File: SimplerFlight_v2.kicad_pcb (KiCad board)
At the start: 4 copper layers, 96 x 73.5 mm, 121 parts, among them J1 Battery 1, J10 Cam 1, J11 Servo, J12 Cam 1, J13 SWD Header, J14 DM3CS-SF, J2 Encoder, J7 Battery 2, J8 USB, J9 Cam 1, Q2 NPN, Q5 BSS816NWH6327XTSA1, Q6 BSS816NWH6327XTSA1, Q7 BSS816NWH6327XTSA1, SW1 Boot Switch, SW2 System Reset, U1 AMS1117-3.3, U2 STM32F401RETx, U3 BMP581, U4 BNO085, U5 TPS56A37RPAR, U6 TPS56A37RPAR, U7 MX25V4006EM1I-13G, Y2 Crystal

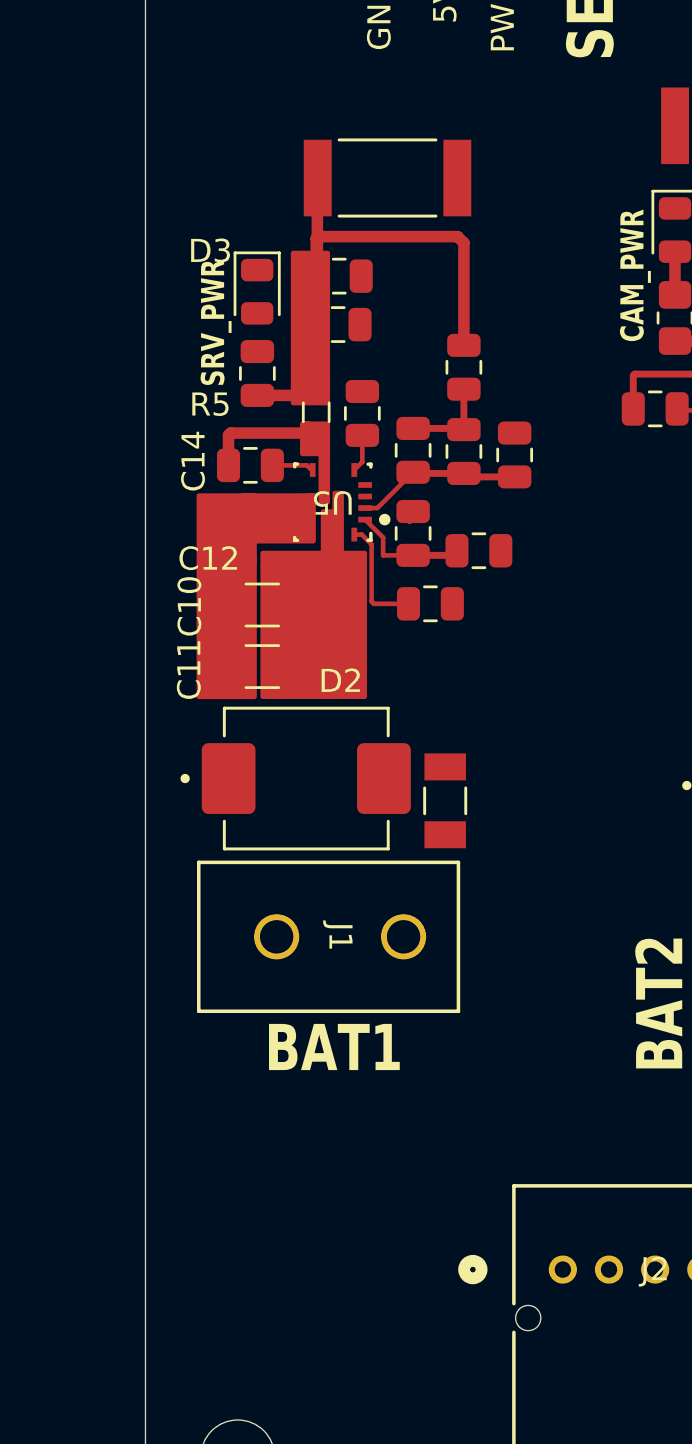
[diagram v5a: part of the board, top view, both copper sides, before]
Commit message: Update Cinx for servo motor power supply
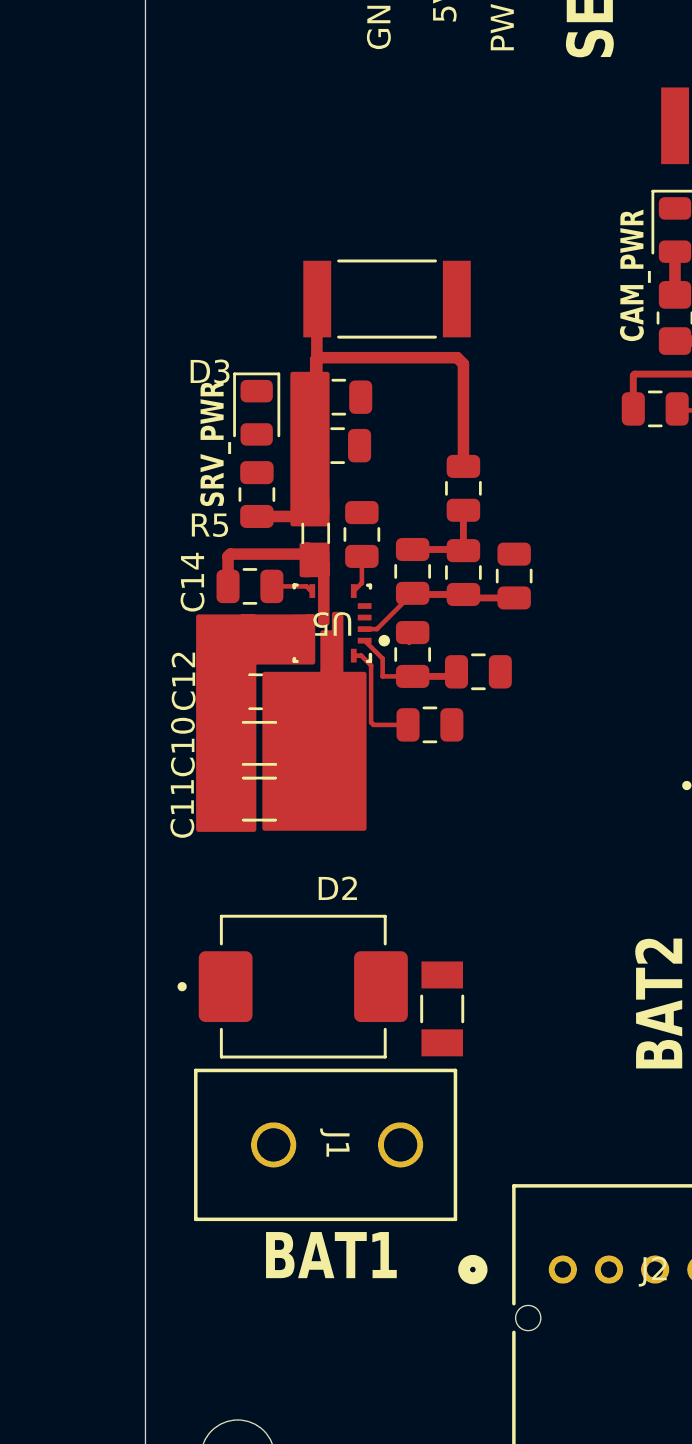
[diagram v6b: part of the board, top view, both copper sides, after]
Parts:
- C12: footprint Capacitor_SMD:C_0201_0603Metric -> Capacitor_SMD:C_0805_2012Metric
- moved F1 9.02 mm to (157.9, 124.6)
- moved J1 9.02 mm to (156.1, 130.5)
- moved D2 9.02 mm to (151.8, 123.6)
- moved C10 6.00 mm to (149.9, 113.1)
- moved C11 5.74 mm to (149.9, 115.5)
- moved C12 5.70 mm to (149.8, 110.8)
- moved C13 5.25 mm to (154.4, 104.0)
- moved C15 5.25 mm to (153.3, 100.2)
- moved C16 5.25 mm to (153.4, 98.1)
- moved D3 5.25 mm to (149.8, 98.8)
- moved L1 5.25 mm to (152.4, 104.0)
- moved R10 5.25 mm to (156.6, 105.6)
- moved R11 5.25 mm to (161.0, 105.8)
- moved R28 5.25 mm to (155.5, 93.8)
- moved R5 5.25 mm to (149.8, 102.3)
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
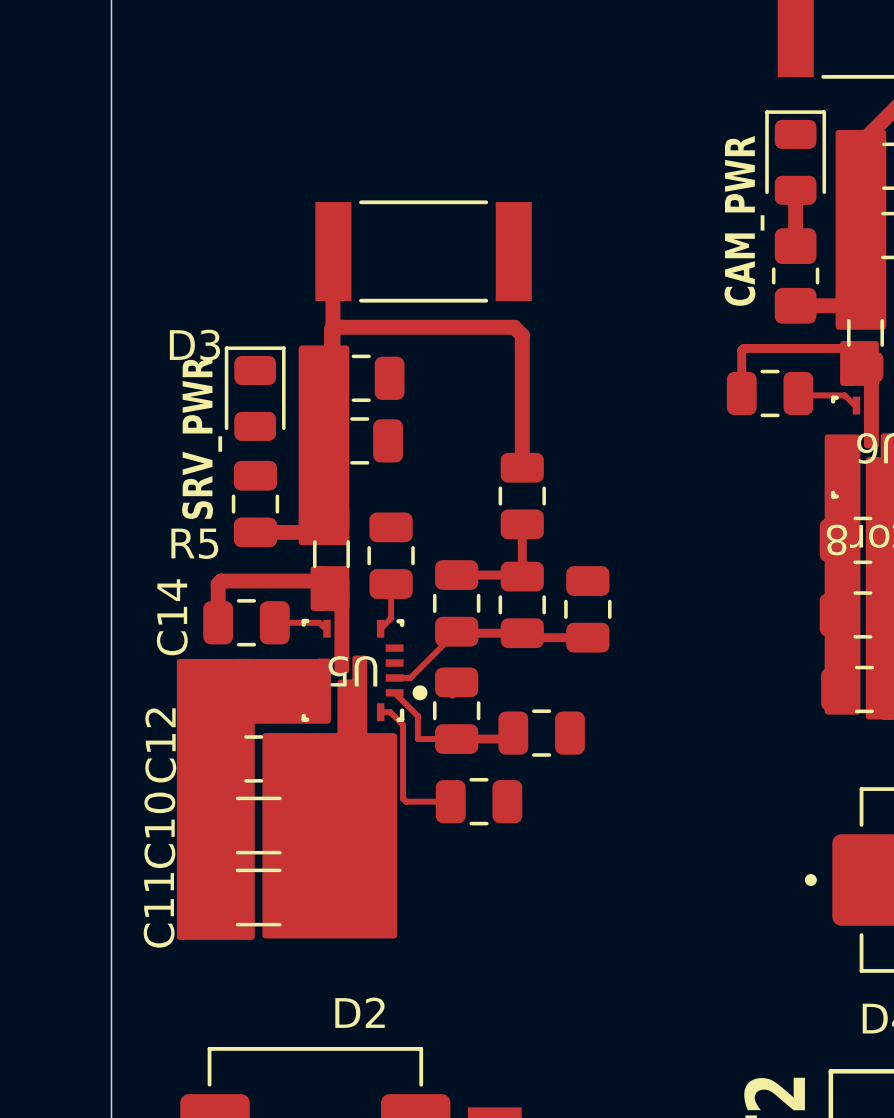
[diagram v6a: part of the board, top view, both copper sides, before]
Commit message: Update Cout models for servo motor power and extended pground
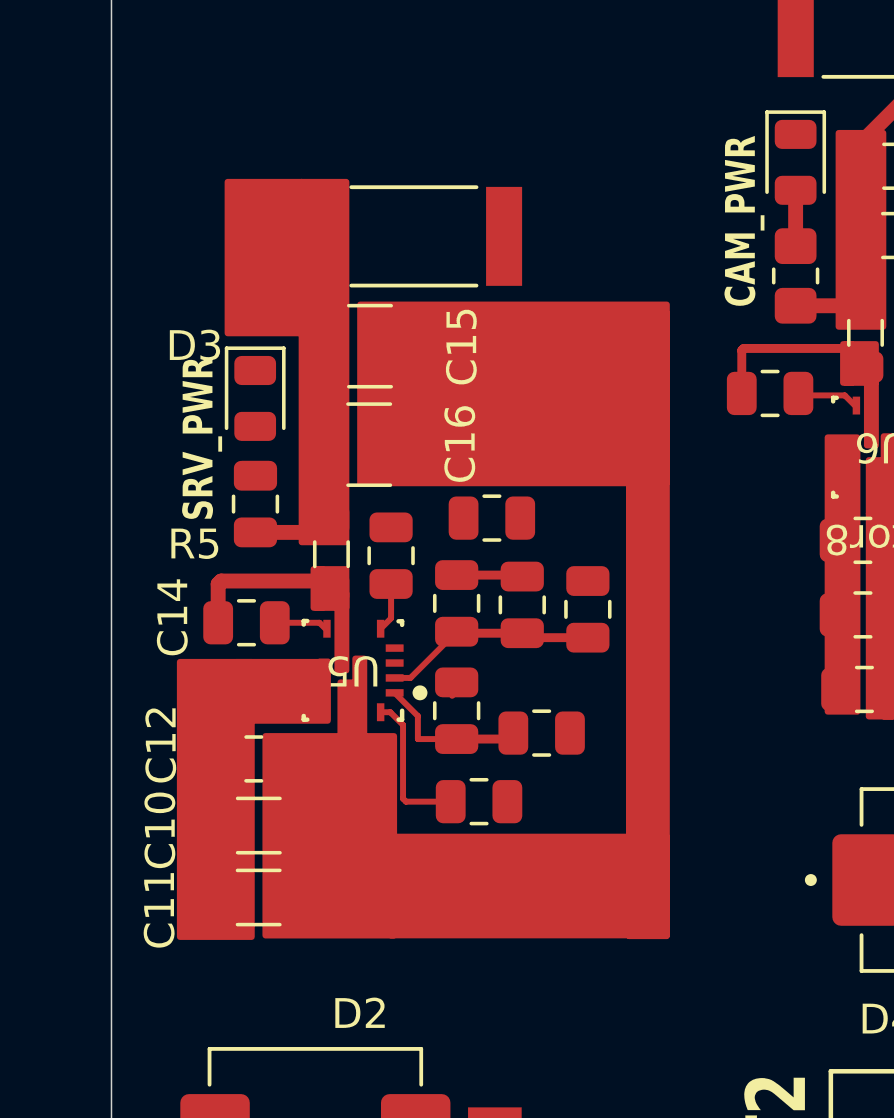
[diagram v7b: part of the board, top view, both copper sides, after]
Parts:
- C15, C16: footprint Capacitor_SMD:C_0805_2012Metric -> Capacitor_SMD:C_1210_3225Metric
- moved C15 3.20 mm to (153.7, 97.0)
- moved C16 2.24 mm to (153.6, 100.3)
- moved R9 1.26 mm to (157.8, 102.8), turned to 0 degrees
- moved R28 0.60 mm to (155.1, 93.3)
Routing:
- net /Power/5V_SERVO: track 21.7 -> 2.72 mm
- net Net-(C17-Pad1): track 3.97 -> 2.22 mm

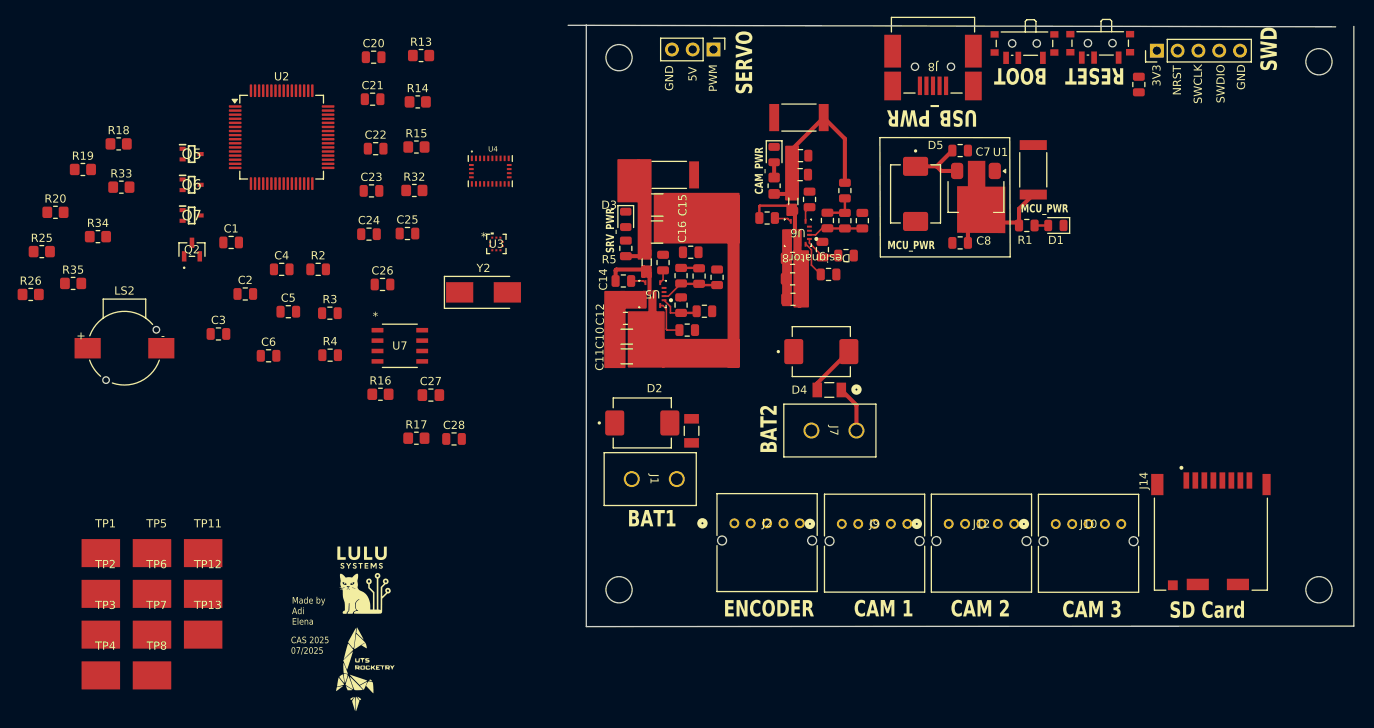
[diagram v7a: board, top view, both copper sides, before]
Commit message: update inductor
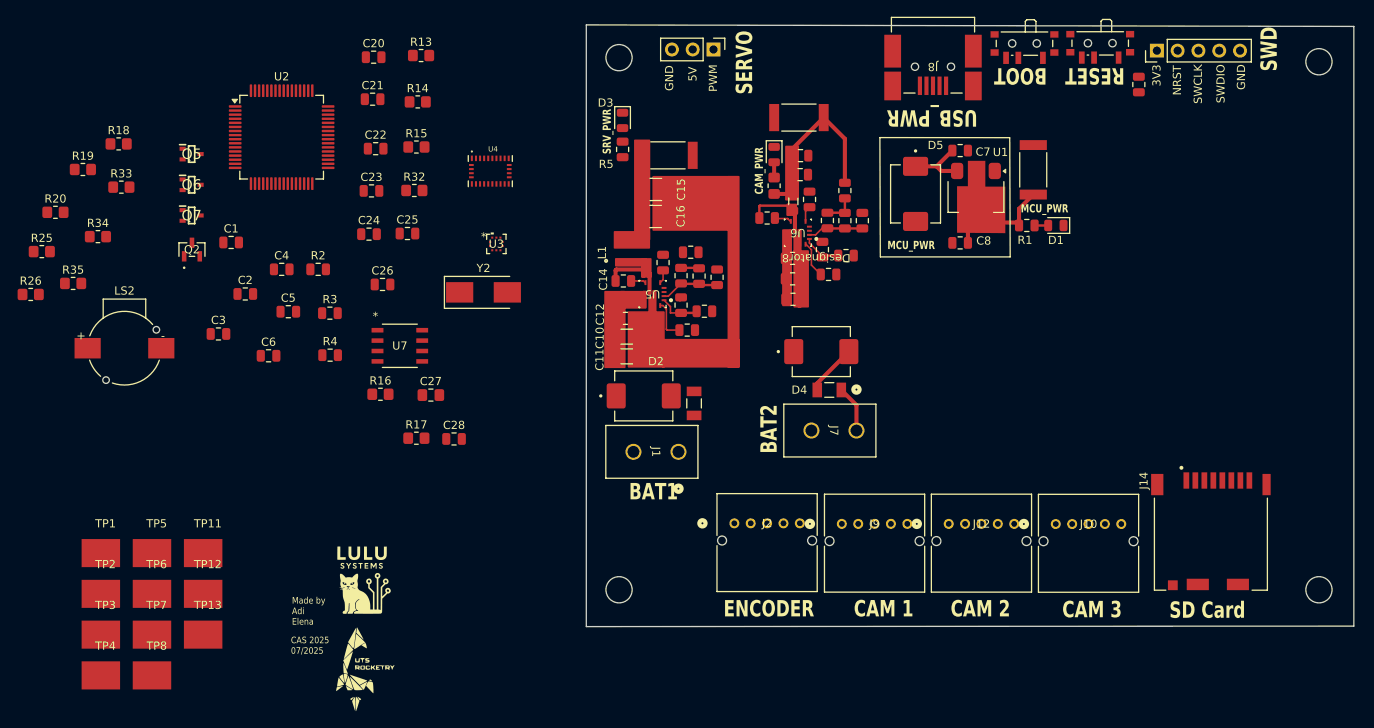
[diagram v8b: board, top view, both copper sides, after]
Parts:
- L1: footprint Inductor_SMD:L_0805_2012Metric_Pad1.05x1.20mm_HandSolder -> 74438357033:WE-MAPI_4030
- moved R5 12.1 mm to (149.4, 90.2)
- moved D3 12.1 mm to (149.4, 86.7)
- moved F1 3.37 mm to (158.2, 121.2)
- moved J1 3.33 mm to (156.3, 127.2)
- moved D2 3.31 mm to (152.0, 120.3)
- moved R28 2.39 mm to (155.0, 90.9)
- moved L1 2.28 mm to (150.4, 102.8)
- moved C15 1.91 mm to (153.5, 95.1)
- moved C16 1.91 mm to (153.5, 98.4)
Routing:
- net /Power/5V_SERVO: track 2.72 -> 0.00 mm
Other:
- board size 96 x 73.5 mm -> 93.8 x 73.5 mm
